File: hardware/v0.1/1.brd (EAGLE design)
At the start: 54.9 x 27.5 mm, 45 parts, among them IC2 STM32F10XCXT6, U1 MIC5219 3.3V, Y1 8MHZ, Y2 32768

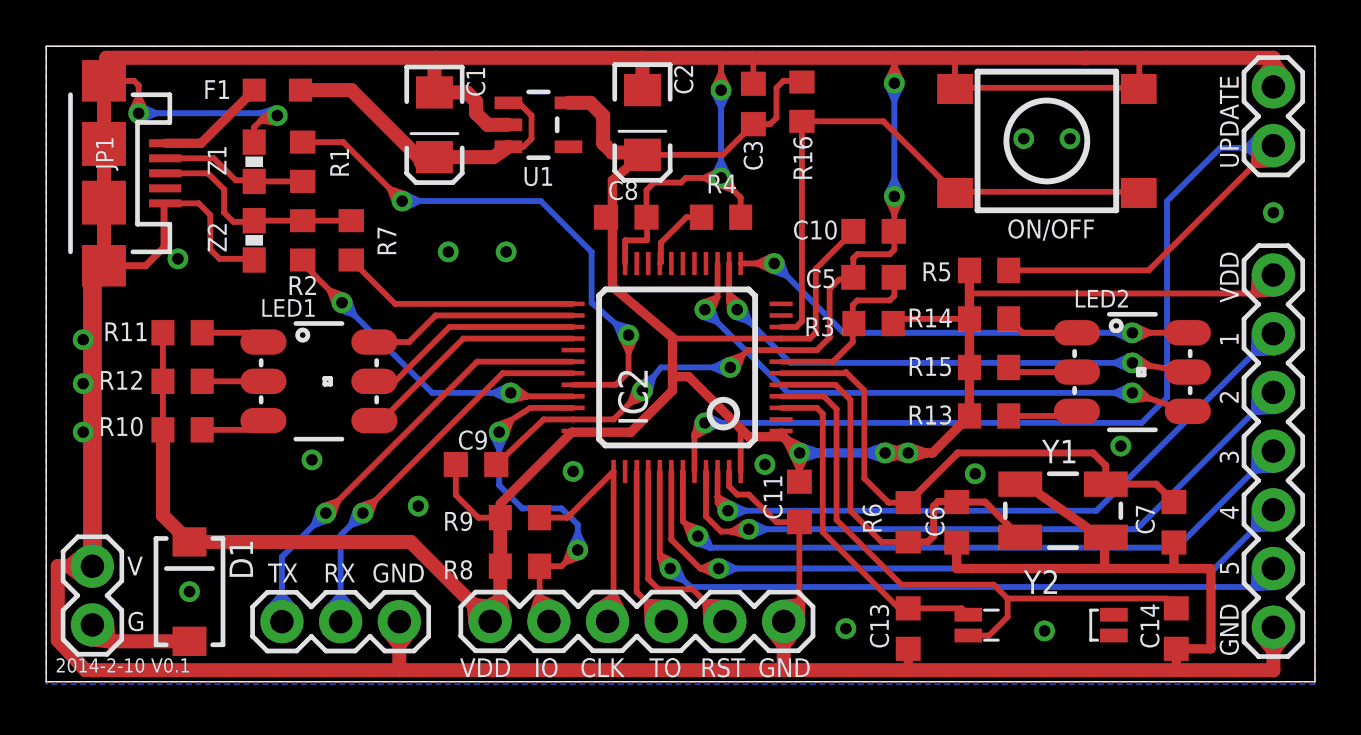
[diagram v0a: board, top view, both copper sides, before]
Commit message: Update readme.md, fix a minor bug on PCB
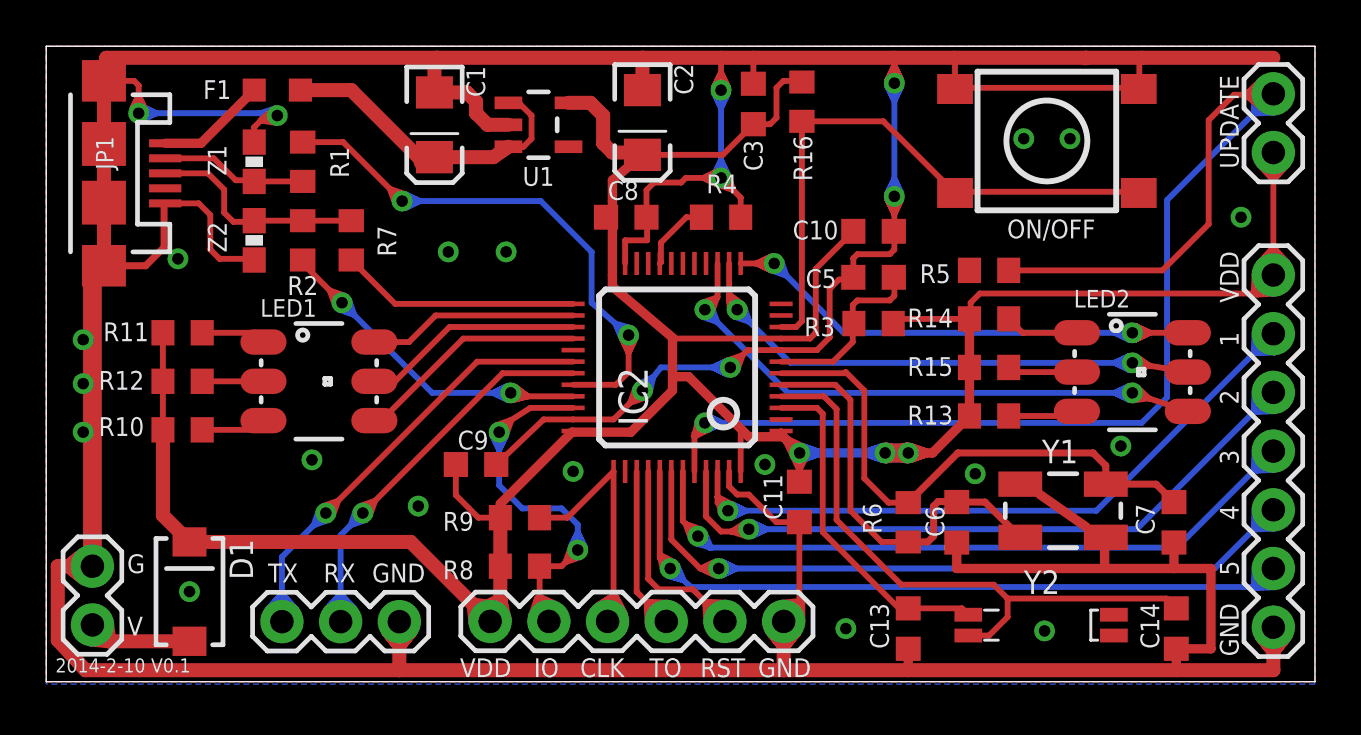
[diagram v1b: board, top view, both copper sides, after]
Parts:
- moved JP5 0.30 mm to (53.1, 22.9)
- turned R5 to 0 degrees
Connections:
- net 3.3V: now also JP5.1; no longer R5.2
- net BOOT0: now also JP5.2, R5.2; no longer JP5.1, R5.1
- net GND: now also R5.1; no longer JP5.2
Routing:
- net GND: track 299.9 -> 356.8 mm
- net 3.3V: track 150.3 -> 199.1 mm
- net LED2_G: track 28.6 -> 40.6 mm
- net USB_DM: track 31.0 -> 40.0 mm
- net BOOT0: track 60.4 -> 68.8 mm
- net SWDIO: track 26.5 -> 34.5 mm
- net GPIO4: track 37.4 -> 45.5 mm
- net USB_DP: track 22.3 -> 28.3 mm
- net USART1_RX: track 23.6 -> 28.0 mm
- net USART1_TX: track 25.8 -> 30.1 mm
- net GPIO1: track 35.6 -> 39.6 mm
- net GPIO2: track 36.1 -> 40.1 mm
- net LED2_B: track 32.8 -> 36.8 mm
- net LED2_R: track 30.6 -> 34.6 mm
- net SWCLK: track 13.5 -> 17.1 mm
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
